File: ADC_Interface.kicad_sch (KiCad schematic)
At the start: 41 parts, among them U2 ADAU1978, X1 12.288MHz

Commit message: (bc) changes for the day
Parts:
- removed C11, C14, C33: 10u, Capacitor_SMD:C_0805_2012Metric_Pad1.18x1.45mm_HandSolder, symbol Device:C_Small
- removed C29: 100n, Capacitor_SMD:C_0603_1608Metric_Pad1.08x0.95mm_HandSolder, symbol Device:C_Small
- removed FB2: BLM18KG101TZ1D, Inductor_SMD:L_0603_1608Metric_Pad1.05x0.95mm_HandSolder, symbol Device:Ferrite_Bead_Small
- removed R1: 10k, Resistor_SMD:R_0603_1608Metric_Pad0.98x0.95mm_HandSolder, symbol Device:R_Small
- removed R92: 47, Resistor_SMD:R_0603_1608Metric_Pad0.98x0.95mm_HandSolder, symbol Device:R_Small
- removed TP1: VADC, TestPoint:TestPoint_Pad_D1.0mm, symbol Connector:TestPoint
- added R101: 2.2k, Resistor_SMD:R_0603_1608Metric_Pad0.98x0.95mm_HandSolder, symbol Device:R_Small
- added R25 (x5): 15, Resistor_SMD:R_0603_1608Metric_Pad0.98x0.95mm_HandSolder, symbol Device:R_Small
- added R36: 10k, Resistor_SMD:R_0603_1608Metric_Pad0.98x0.95mm_HandSolder, symbol Device:R_Small
- R13, R19: value 100k -> 10k; MPN RC0603FR-07100KL -> (none)
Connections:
- net +3V3: now also R36.2
- net CLK: now also R25.1
- net GNDA: now also R101.2
- net SAI_BCLK: now also R25.1; no longer U2.16 (BCLK)
- net SAI_FCLK: now also R25.1; no longer U2.15 (LRCLK)
- net SAI_SD1: now also R25.1; no longer U2.13 (SDATAOUT1)
- net SAI_SD2: now also R25.1; no longer U2.14 (SDATAOUT2)
- net at X1.3 (OUT): now also R25.2
- net +1V8 renamed ADC_VDD
- net ADC_VDD: now also R101.1
- net ~{RST}: no longer names the net of U2.6 (~{RST/PD})
- net ~{RST}: now also R36.1
- new net: R25.2, U2.13 (SDATAOUT1)
- new net: R25.2, U2.14 (SDATAOUT2)
- new net: R25.2, U2.15 (LRCLK)
- new net: R25.2, U2.16 (BCLK)
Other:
- note added: "R_{EXT} required fro correct reset behaviour. See ADC datasheet, power-on reset section."
- note added: "See `scripts/compute_adc_clock.jl` for more info"
- note added: "Series termination resistors, place close to ADC (Bus master)"
- note added: "Tie close to AVDD2"
- note removed: "Local ~{RST} Pull Down"
- note removed: "TODO: REPLACE WITH ANALOGUE REFERENCE AND LOTS OF CAPACITANCE"
- moved on the sheet: C10, C12, C13, C15, C16, C17, C20, C21, C22, C23, C24, C25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

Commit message: (sch) relabel
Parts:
- renumbered C10 to C401, C13 to C402, C12 to C403, C32 to C404, C15 to C405, C16 to C406, C17 to C407, C28 to C408, C20 to C409, C21 to C410, C22 to C411, C23 to C412, C24 to C413, C25 to C414, CB16 to CB401, JP6 to JP401, JP7 to JP402, R13 to R401, R19 to R402, R11 to R404, R12 to R406, R14 to R407, R15 to R408, R36 to R413, R16 to R414, TP6 to TP401, TP7 to TP402, TP8 to TP403, TP2 to TP404, TP9 to TP405, TP10 to TP406, TP11 to TP407, U2 to U401, X1 to X401

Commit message: (bc) finish up ERC
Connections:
- net GNDD is gone; now on net GND: C403.2, CB401.2, U401.11 (DGND), X401.2 (GND)
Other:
- sheet Sensor_Conn_1 ports: added 3v3A, GND; removed none
- sheet Sensor_Conn_2 ports: added 3v3A, GND; removed none

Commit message: (sch) change 2.2k R to 0402
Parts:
- R101: footprint Resistor_SMD:R_0603_1608Metric_Pad0.98x0.95mm_HandSolder -> Resistor_SMD:R_0402_1005Metric; MPN RC0603FR-072K2L -> RT0402FRE072K2L
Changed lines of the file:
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@@
       (effects (font (size 1.27 1.27)) (justify left))
     )
-    (property "Footprint" "Resistor_SMD:R_0603_1608Metric_Pad0.98x0.95mm_HandSolder" (at 129.54 38.735 0)
+    (property "Footprint" "Resistor_SMD:R_0402_1005Metric" (at 129.54 38.735 0)
       (effects (font (size 1.27 1.27)) hide)
     )
@@
       (effects (font (size 1.27 1.27)) hide)
     )
-    (property "MPN" "RC0603FR-072K2L" (at 129.54 38.735 0)
+    (property "MPN" "RT0402FRE072K2L" (at 129.54 38.735 0)
       (effects (font (size 1.27 1.27)) hide)
     )

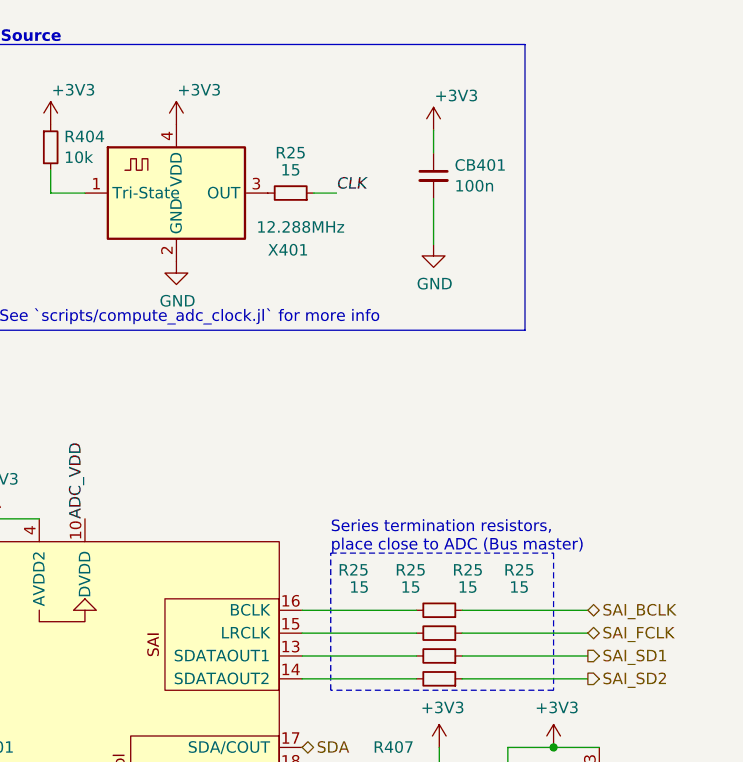
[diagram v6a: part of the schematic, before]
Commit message: (sch) change passives to 0402
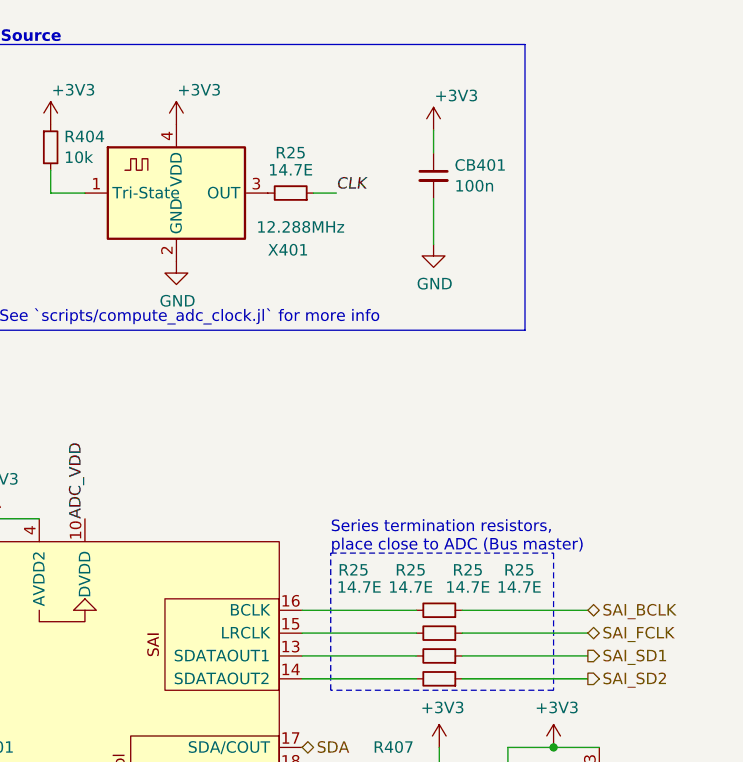
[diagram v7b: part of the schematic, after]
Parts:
- C413: footprint Capacitor_SMD:C_0603_1608Metric_Pad1.08x0.95mm_HandSolder -> Capacitor_SMD:C_0402_1005Metric; MPN CC0603JRX7R9BB562 -> GRM1555C1H562JE01D; Mfr. Yageo -> Murata
- C414: footprint Capacitor_SMD:C_0603_1608Metric_Pad1.08x0.95mm_HandSolder -> Capacitor_SMD:C_0402_1005Metric; MPN CC0603JRNPO9BN391 -> GRM1555C1H391JA01D; Mfr. Yageo -> Murata
- R25: value 15 -> 14.7E; footprint Resistor_SMD:R_0603_1608Metric_Pad0.98x0.95mm_HandSolder -> Resistor_SMD:R_0402_1005Metric; MPN ERJ-3EKF15R0V -> RT0603FRE0714R7L; Mfr. Panasonic -> Yageo
- R401, R402: footprint Resistor_SMD:R_0603_1608Metric_Pad0.98x0.95mm_HandSolder -> Resistor_SMD:R_0402_1005Metric; MPN (none) -> RT0402FRE1310KL
- R404, R406, R407, R408, R413: footprint Resistor_SMD:R_0603_1608Metric_Pad0.98x0.95mm_HandSolder -> Resistor_SMD:R_0402_1005Metric; MPN RC0603JR-0710KL -> RT0402FRE1310KL
- R414: footprint Resistor_SMD:R_0603_1608Metric_Pad0.98x0.95mm_HandSolder -> Resistor_SMD:R_0402_1005Metric; MPN RC0603FR-071KL -> RT0402FRE071KL

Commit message: (pcb) initial layout
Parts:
- removed R25 (x2): 14.7E, Resistor_SMD:R_0402_1005Metric, symbol Device:R_Small
- C405, C406, C407, C408, C410, C412, CB401: footprint Capacitor_SMD:C_0603_1608Metric_Pad1.08x0.95mm_HandSolder -> Capacitor_SMD:C_0402_1005Metric; MPN C0603C104M5RACTU -> C0402C104K8PACTU
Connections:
- net SAI_FCLK: now also U401.15 (LRCLK)
- net SDATA: now reaches R25.2, U401.13 (SDATAOUT1)
- net BCLK: now reaches R25.2, U401.16 (BCLK)
- net ADC_~{RST}: now reaches R413.1, U401.6 (~{RST/PD})
- net SA_MODE: now reaches R406.2, U401.9 (SA_MODE)
- no-connect marks 0 -> 1
